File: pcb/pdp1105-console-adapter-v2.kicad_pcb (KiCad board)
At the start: 2 copper layers, 72 x 52 mm, 15 parts, among them J1 SCL Connector, J2 Aux Terminal Connector, Q1 MMBT3904, U1 Pico, U2 MAX3232

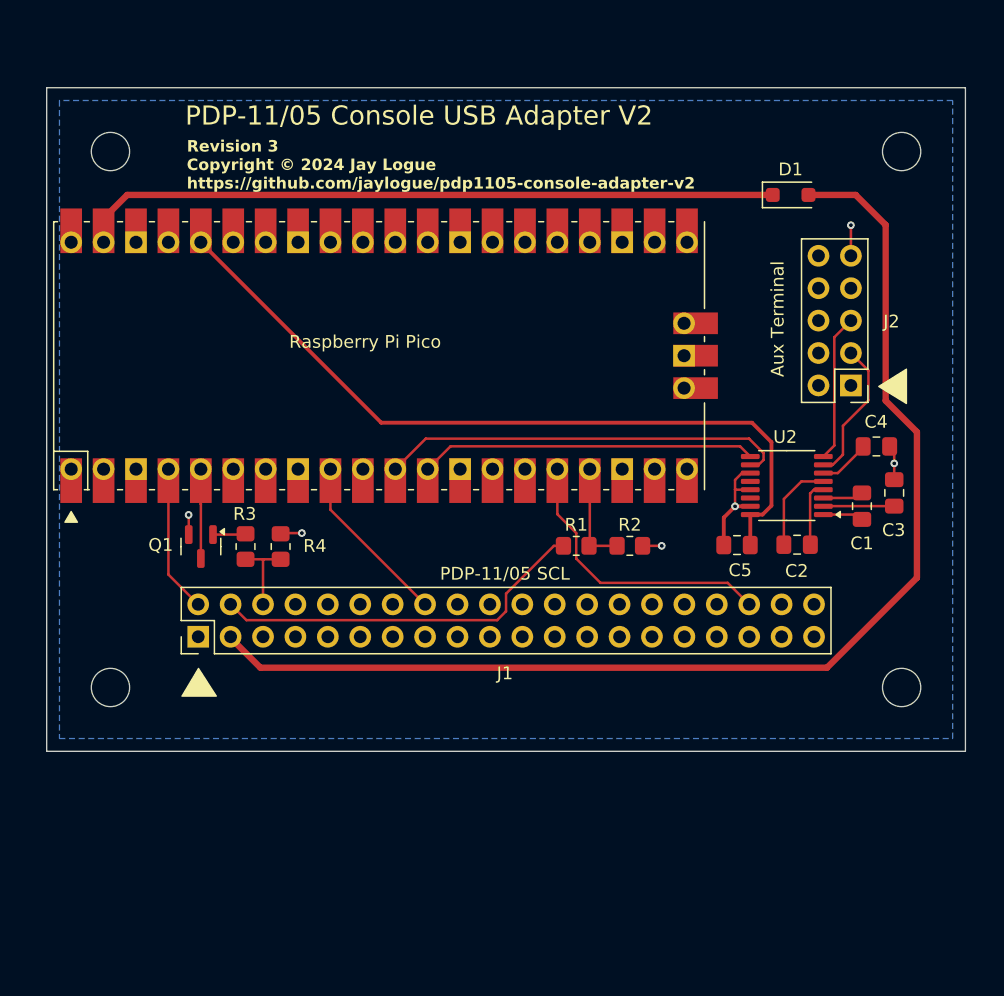
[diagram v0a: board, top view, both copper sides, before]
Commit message: ﻿Initial version of Rev 4 schematic
-- Added status LEDs

-- Changed Aux port connector to board-mounted DE9

-- Added mounting hole components
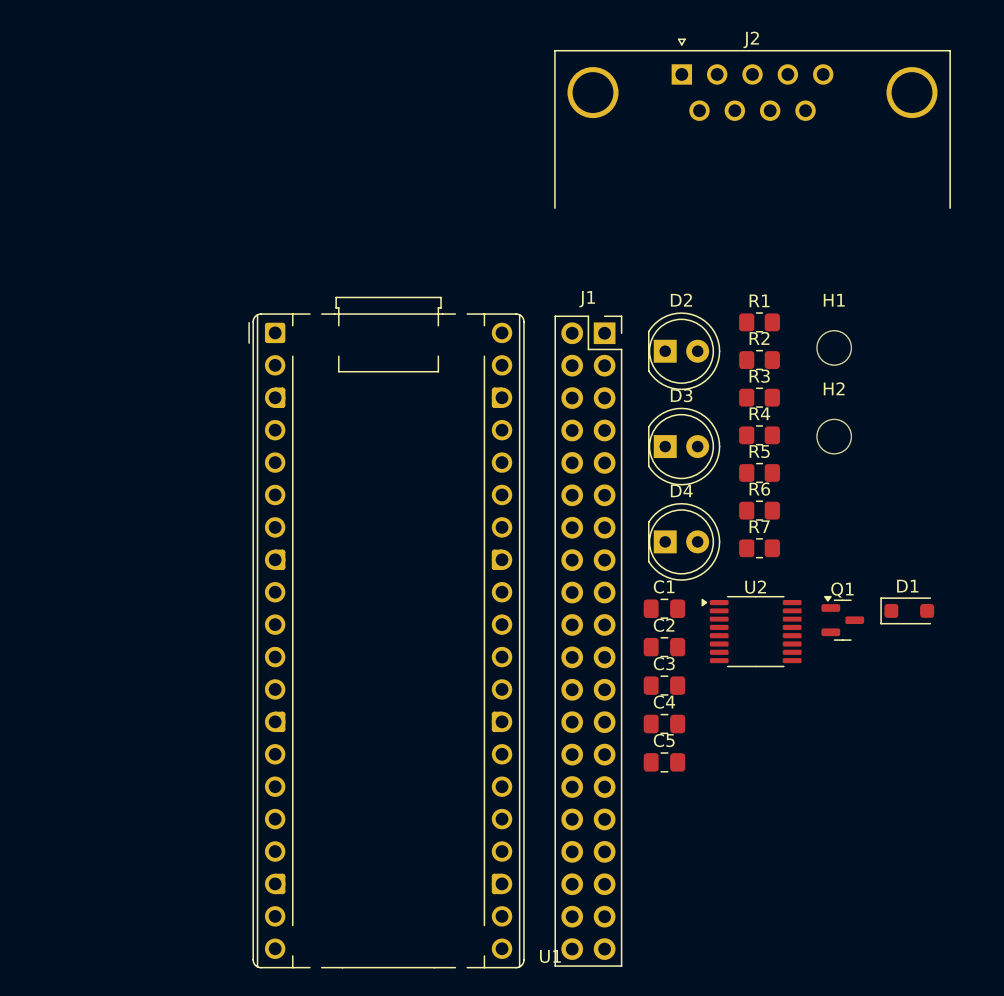
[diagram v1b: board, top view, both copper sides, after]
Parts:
- added D2: LED, LED_THT:LED_D5.0mm, F.Cu at (153.6, 90.2)
- added D3: LED, LED_THT:LED_D5.0mm, F.Cu at (153.6, 97.7)
- added D4: LED, LED_THT:LED_D5.0mm, F.Cu at (153.6, 105.1)
- added H1: MountingHole, MountingHole:MountingHole_2.7mm_M2.5, F.Cu at (166.9, 89.9)
- added H2: MountingHole, MountingHole:MountingHole_2.7mm_M2.5, F.Cu at (166.9, 96.9)
- added R5: 220, Resistor_SMD:R_0805_2012Metric_Pad1.20x1.40mm_HandSolder, F.Cu at (161.0, 99.7)
- added R6: 220, Resistor_SMD:R_0805_2012Metric_Pad1.20x1.40mm_HandSolder, F.Cu at (161.0, 102.7)
- added R7: 220, Resistor_SMD:R_0805_2012Metric_Pad1.20x1.40mm_HandSolder, F.Cu at (161.0, 105.6)
- J1: footprint Connector_PinHeader_2.54mm:PinHeader_2x20_P2.54mm_Vertical -> Connector_PinSocket_2.54mm:PinSocket_2x20_P2.54mm_Vertical
- J2: value Aux Terminal Connector -> DE9_Plug; footprint Connector_PinHeader_2.54mm:PinHeader_2x05_P2.54mm_Vertical -> Connector_Dsub:DSUB-9_Male_Horizontal_P2.77x2.84mm_EdgePinOffset7.70mm_Housed_MountingHolesOffset9.12mm
- U1: footprint MCU_RaspberryPi_and_Boards:RPi_Pico_SMD_TH -> Module:RaspberryPi_Pico_Common_THT
- moved Q1 50.6 mm to (167.6, 111.3), turned to 0 degrees
- moved R3 41.9 mm to (161.0, 93.8), turned to 0 degrees
- moved J1 39.8 mm to (148.9, 88.8), turned to 0 degrees
- moved R4 38.5 mm to (161.0, 96.8), turned to 0 degrees
- moved D1 33.9 mm to (172.8, 110.5)
- moved J2 27.7 mm to (154.9, 68.5), turned to 0 degrees
- moved C4 27.4 mm to (153.6, 119.4)
- moved C3 23.5 mm to (153.6, 116.4), turned to 0 degrees
- moved R1 22.6 mm to (161.0, 87.9)
- moved C5 18.0 mm to (153.6, 122.4), turned to 0 degrees
- moved R2 17.8 mm to (161.0, 90.9)
- moved C1 17.4 mm to (153.6, 110.4), turned to 0 degrees
- moved C2 13.1 mm to (153.6, 113.4), turned to 0 degrees
- moved U2 11.7 mm to (160.7, 112.2), turned to 0 degrees
- moved U1 8.34 mm to (123.1, 88.8), turned to 0 degrees
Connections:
- U1 pad 1: unconnected-(U1-GPIO0-Pad1) -> TX_LED
- U1 pad 2: unconnected-(U1-GPIO1-Pad2) -> RX_LED
- U1 pad 6: unconnected-(U1-GPIO4-Pad6) -> STATUS_LED
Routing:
- net +5V: track 93.5 -> 0.00 mm
- net +3V3: track 60.7 -> 0.00 mm
- net Net-(D1-K): track 55.1 -> 0.00 mm
- net AUX_TERM_TX: track 32.0 -> 0.00 mm
- net SERIAL_OUT_TTL: track 29.8 -> 0.00 mm
- net AUX_TERM_RX: track 26.4 -> 0.00 mm
- net SERIAL_IN_TTL: track 22.7 -> 0.00 mm
- net GND: track 19.1 -> 0.00 mm, vias 6 -> 0
- net CLK_IN: track 13.7 -> 0.00 mm
- net SCL_DETECT: track 11.6 -> 0.00 mm
- net Net-(U2-R2IN): track 11.5 -> 0.00 mm
- net Net-(U2-T2OUT): track 11.2 -> 0.00 mm
- net Net-(U1-GPIO13): track 8.24 -> 0.00 mm
- net Net-(U2-C2-): track 7.25 -> 0.00 mm
- net READER_RUN_3V3: track 7.00 -> 0.00 mm
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- removed copper zone on B.Cu, net GND
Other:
- board outline removed
- board text removed: "Aux Terminal"
- board text removed: "PDP-11/05 Console USB Adapter V2"
- board text removed: "PDP-11/05 SCL"
- board text removed: "Raspberry Pi Pico"
- board text removed: "Revision 3 Copyright © 2024 Jay Logue https://github.com/jaylogue/pdp1105-console-adapter-v2"

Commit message: ﻿Initial version of Rev 4 PCB
-- New PCB board outline

-- Basic placement of major components: Pico, SCL connector, DE9, LEDs and
mounting holes.

-- No other components placed.  No traces routed.
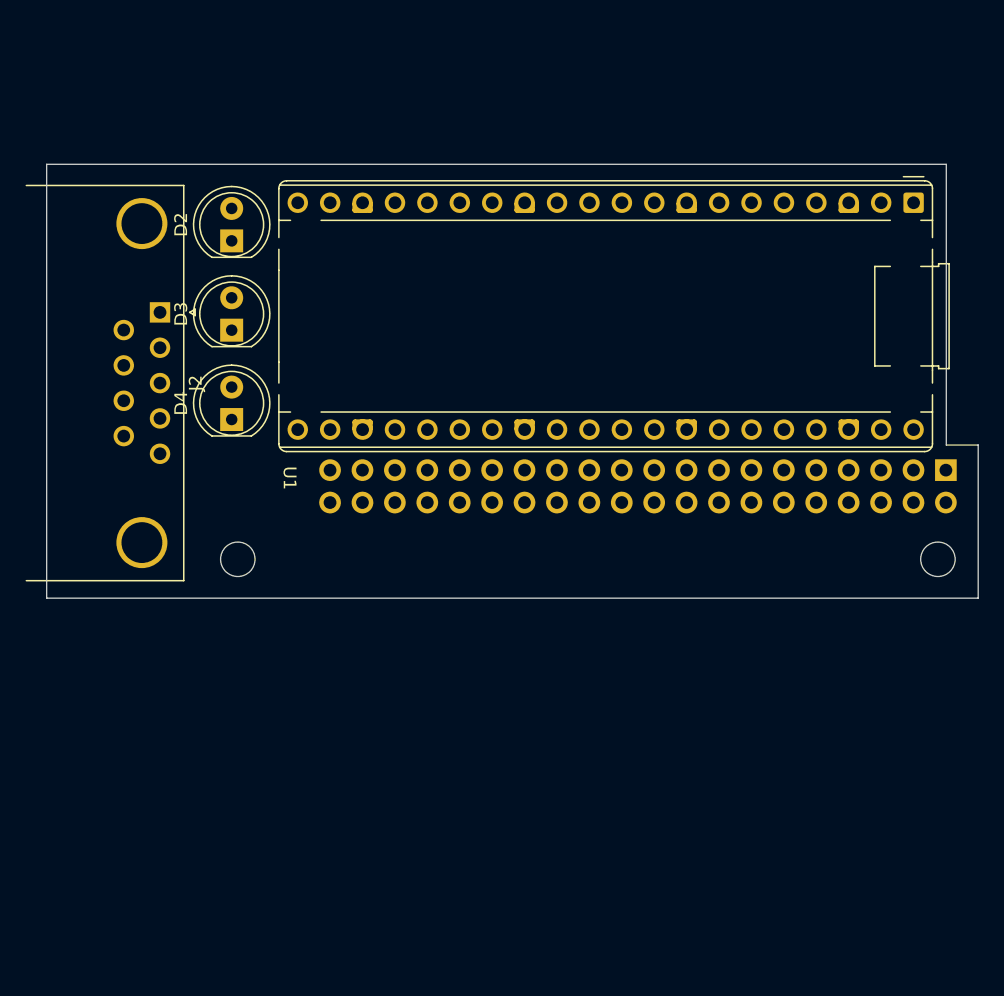
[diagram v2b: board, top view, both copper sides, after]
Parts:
- removed C1, C2, C3, C4, C5: 0.1uF, Capacitor_SMD:C_0805_2012Metric_Pad1.18x1.45mm_HandSolder
- removed D1: MBR1020VL, Diode_SMD:D_SOD-123F
- removed Q1: MMBT3904, Package_TO_SOT_SMD:SOT-23
- removed R1: 5.1K, Resistor_SMD:R_0805_2012Metric_Pad1.20x1.40mm_HandSolder
- removed R2: 10K, Resistor_SMD:R_0805_2012Metric_Pad1.20x1.40mm_HandSolder
- removed R3, R4: 1K, Resistor_SMD:R_0805_2012Metric_Pad1.20x1.40mm_HandSolder
- removed R5, R6, R7: 220, Resistor_SMD:R_0805_2012Metric_Pad1.20x1.40mm_HandSolder
- removed U2: MAX3232, Package_SO:TSSOP-16_4.4x5mm_P0.65mm
- J1: moved to B.Cu
- moved U1 51.1 mm to (173.1, 78.6), turned to -90 degrees
- moved H2 47.7 mm to (120.1, 106.5)
- moved J2 44.9 mm to (114.0, 87.2), turned to -90 degrees
- moved D4 35.3 mm to (119.7, 95.5), turned to 90 degrees
- moved D3 35.2 mm to (119.7, 88.5), turned to 90 degrees
- moved D2 35.1 mm to (119.7, 81.5), turned to 90 degrees
- moved J1 28.8 mm to (175.6, 99.5), turned to 90 degrees
- moved H1 18.4 mm to (175.0, 106.5)
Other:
- board outline added: 73 x 34 mm

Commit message: ﻿Completed layout and routing for revision 4 PCB
-- NOTE: Pico pin assignments were altered from revision 3 board to simplify routing
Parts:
- added C1: 0.1uF, Capacitor_SMD:C_0805_2012Metric_Pad1.18x1.45mm_HandSolder, F.Cu at (139.7, 84.6)
- added C2: 0.1uF, Capacitor_SMD:C_0805_2012Metric_Pad1.18x1.45mm_HandSolder, F.Cu at (139.7, 88.7)
- added C3: 0.1uF, Capacitor_SMD:C_0805_2012Metric_Pad1.18x1.45mm_HandSolder, F.Cu at (136.4, 85.6)
- added C4: 0.1uF, Capacitor_SMD:C_0805_2012Metric_Pad1.18x1.45mm_HandSolder, F.Cu at (136.4, 89.8)
- added C5: 0.1uF, Capacitor_SMD:C_0805_2012Metric_Pad1.18x1.45mm_HandSolder, F.Cu at (153.0, 84.6)
- added D1: MBR1020VL, Diode_SMD:D_SOD-123F, F.Cu at (170.5, 92.0)
- added Q1: MMBT3904, Package_TO_SOT_SMD:SOT-23, F.Cu at (162.9, 84.2)
- added R1: 5.1K, Resistor_SMD:R_0805_2012Metric_Pad1.20x1.40mm_HandSolder, F.Cu at (170.4, 85.4)
- added R2: 10K, Resistor_SMD:R_0805_2012Metric_Pad1.20x1.40mm_HandSolder, F.Cu at (170.4, 83.2)
- added R3: 1K, Resistor_SMD:R_0805_2012Metric_Pad1.20x1.40mm_HandSolder, F.Cu at (162.9, 88.2)
- added R4: 1K, Resistor_SMD:R_0805_2012Metric_Pad1.20x1.40mm_HandSolder, F.Cu at (162.9, 90.5)
- added R5: 220, Resistor_SMD:R_0805_2012Metric_Pad1.20x1.40mm_HandSolder, F.Cu at (126.4, 83.2)
- added R6: 220, Resistor_SMD:R_0805_2012Metric_Pad1.20x1.40mm_HandSolder, F.Cu at (126.4, 85.9)
- added R7: 220, Resistor_SMD:R_0805_2012Metric_Pad1.20x1.40mm_HandSolder, F.Cu at (126.4, 92.0)
- added U2: MAX3232, Package_SO:SOIC-16_3.9x9.9mm_P1.27mm, F.Cu at (146.4, 87.7)
- U1: footprint Module:RaspberryPi_Pico_Common_THT -> pdp1105-console-adapter:RaspberryPi_Pico_Common_THT
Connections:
- J1 pad 2: SCL_DETECT -> GND
- J1 pad 39: GND -> SCL_DETECT
- U1 pad 1: TX_LED -> unconnected-(U1-GPIO0-Pad1)
- U1 pad 16: SERIAL_IN_TTL -> unconnected-(U1-GPIO12-Pad16)
- U1 pad 17: Net-(U1-GPIO13) -> unconnected-(U1-GPIO13-Pad17)
- U1 pad 19: unconnected-(U1-GPIO14-Pad19) -> STATUS_LED
- U1 pad 2: RX_LED -> Net-(U1-GPIO1)
- U1 pad 20: unconnected-(U1-GPIO15-Pad20) -> TX_LED
- U1 pad 21: unconnected-(U1-GPIO16-Pad21) -> SERIAL_IN_TTL
- U1 pad 22: unconnected-(U1-GPIO17-Pad22) -> RX_LED
- U1 pad 24: unconnected-(U1-GPIO18-Pad24) -> SCL_DETECT
- U1 pad 29: unconnected-(U1-GPIO22-Pad29) -> CLK_IN
- U1 pad 4: SCL_DETECT -> unconnected-(U1-GPIO2-Pad4)
- U1 pad 6: STATUS_LED -> unconnected-(U1-GPIO4-Pad6)
- U1 pad 9: CLK_IN -> unconnected-(U1-GPIO6-Pad9)
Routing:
- net Net-(U2-R2IN): track 0.00 -> 31.9 mm
- net Net-(U2-T2OUT): track 0.00 -> 31.3 mm
- net +3V3: track 0.00 -> 21.9 mm
- net GND: track 0.00 -> 20.0 mm, vias 0 -> 5
- net SERIAL_OUT_TTL: track 0.00 -> 19.3 mm
- net READER_RUN+: track 0.00 -> 17.7 mm
- net CLK_IN: track 0.00 -> 16.3 mm
- net AUX_TERM_RX: track 0.00 -> 15.8 mm
- net SERIAL_IN_TTL: track 0.00 -> 14.3 mm
- net AUX_TERM_TX: track 0.00 -> 14.2 mm
- net TX_LED: track 0.00 -> 8.43 mm
- net Net-(U2-VS-): track 0.00 -> 8.01 mm
- net +5V: track 0.00 -> 7.98 mm
- net Net-(U2-VS+): track 0.00 -> 7.51 mm
- net Net-(D2-A): track 0.00 -> 7.46 mm
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- added copper zone on B.Cu, net GND
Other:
- board text added: "PDP-11/05 Console Adapter V2"
- board text added: "Revision 4 Copyright © 2025 Jay Logue"
- board text added: "https://github.com/jaylogue/pdp1105-console-adapter-v2"

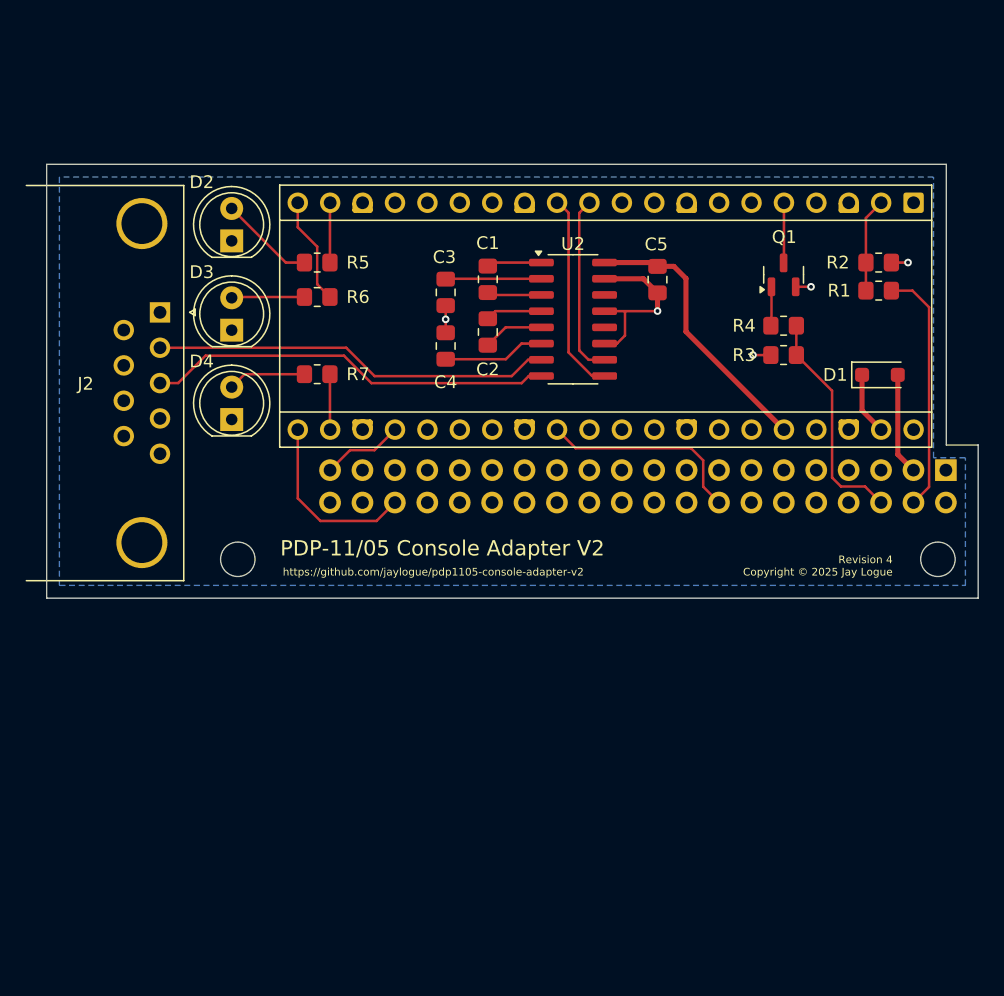
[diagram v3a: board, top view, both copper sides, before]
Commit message: ﻿Updates to rev 4 PCB layout
-- Moved SMT components to back side of PCB to facilitate rework when Pico
is soldered in place.
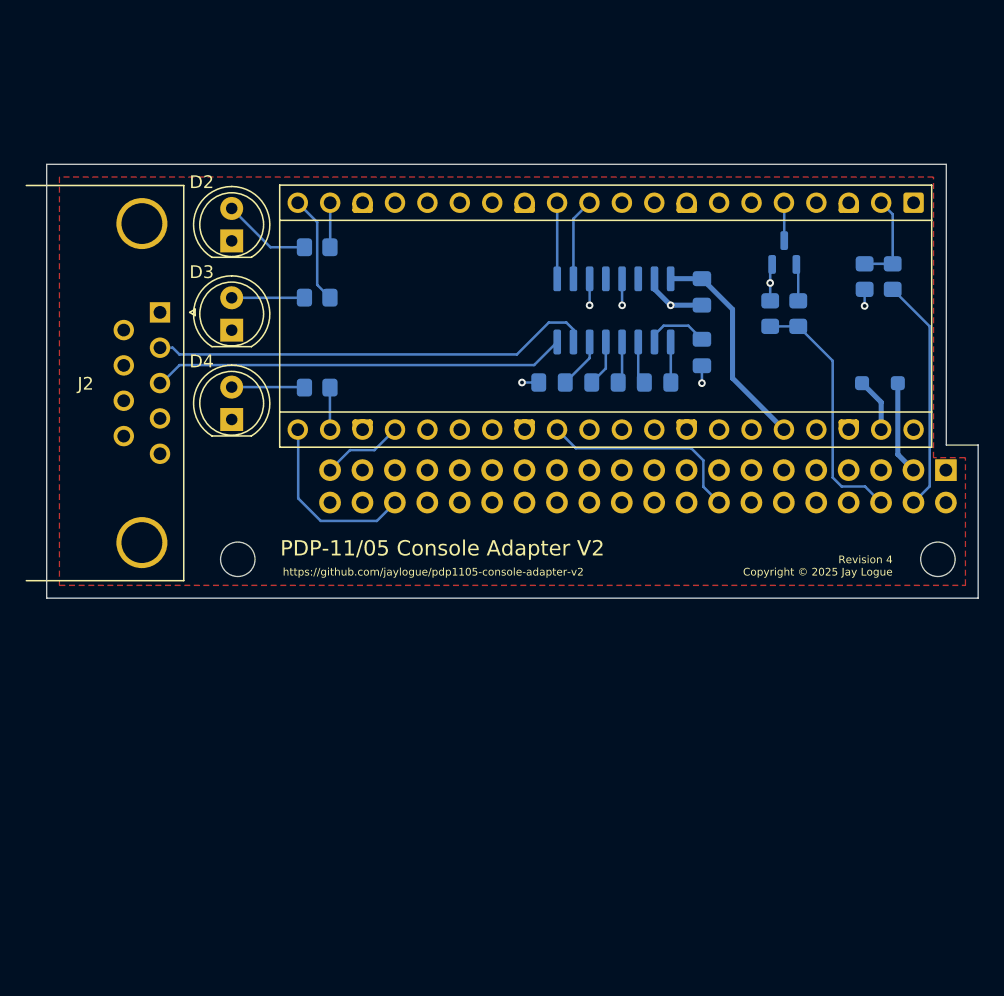
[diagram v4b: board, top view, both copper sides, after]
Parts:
- C1, C2, C3, C4, C5, D1, Q1, R1, R2, R3, R4, R5, R6, R7, U2: moved to B.Cu
- moved C3 20.6 mm to (156.5, 90.3)
- moved C1 15.6 mm to (153.0, 92.6), turned to 180 degrees
- moved C2 10.00 mm to (148.9, 92.6), turned to 180 degrees
- moved C4 8.81 mm to (144.8, 92.6), turned to 180 degrees
- moved C5 3.61 mm to (156.5, 85.5)
- moved R4 3.42 mm to (161.9, 87.2), turned to -90 degrees
- moved U2 3.28 mm to (149.6, 87.0), turned to 90 degrees
- moved Q1 1.75 mm to (163.0, 82.5)
- moved R2 1.56 mm to (169.3, 84.3), turned to -90 degrees
- moved R1 1.56 mm to (171.5, 84.3), turned to 90 degrees
- moved R3 1.49 mm to (164.1, 87.2), turned to 90 degrees
- moved R5 1.20 mm to (126.4, 82.0)
- moved R7 1.05 mm to (126.4, 93.0)
- moved D1 0.65 mm to (170.5, 92.7)
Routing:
- net AUX_TERM_RX: track 15.8 -> 5.97 mm
- net AUX_TERM_TX: track 14.2 -> 6.48 mm
- net +3V3: track 21.9 -> 16.9 mm
- net Net-(U2-VS-): track 8.01 -> 3.97 mm
- net GND: track 20.0 -> 16.1 mm, vias 5 -> 7
- net Net-(U2-T2OUT): track 31.3 -> 34.9 mm
- net Net-(U2-VS+): track 7.51 -> 5.01 mm
- net READER_RUN+: track 17.7 -> 19.8 mm
- net READER_RUN_3V3: track 4.72 -> 2.97 mm
- net STATUS_LED: track 4.70 -> 3.50 mm
- net Net-(U2-C2-): track 4.78 -> 3.63 mm
- net Net-(U2-C2+): track 4.44 -> 3.31 mm
- net Net-(U2-C1+): track 4.31 -> 3.18 mm
- net RX_LED: track 4.35 -> 3.30 mm
- net Net-(U2-C1-): track 4.28 -> 3.37 mm
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- added copper zone on F.Cu, net GND
- removed copper zone on B.Cu, net GND
